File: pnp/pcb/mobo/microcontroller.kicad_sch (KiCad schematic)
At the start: 34 parts, among them J1 SWD Header, J32 BOOT_JUMPER, SW1 SW_Push, SW2 SW_Push, U1 STM32F407VETx, Y1 8MHz

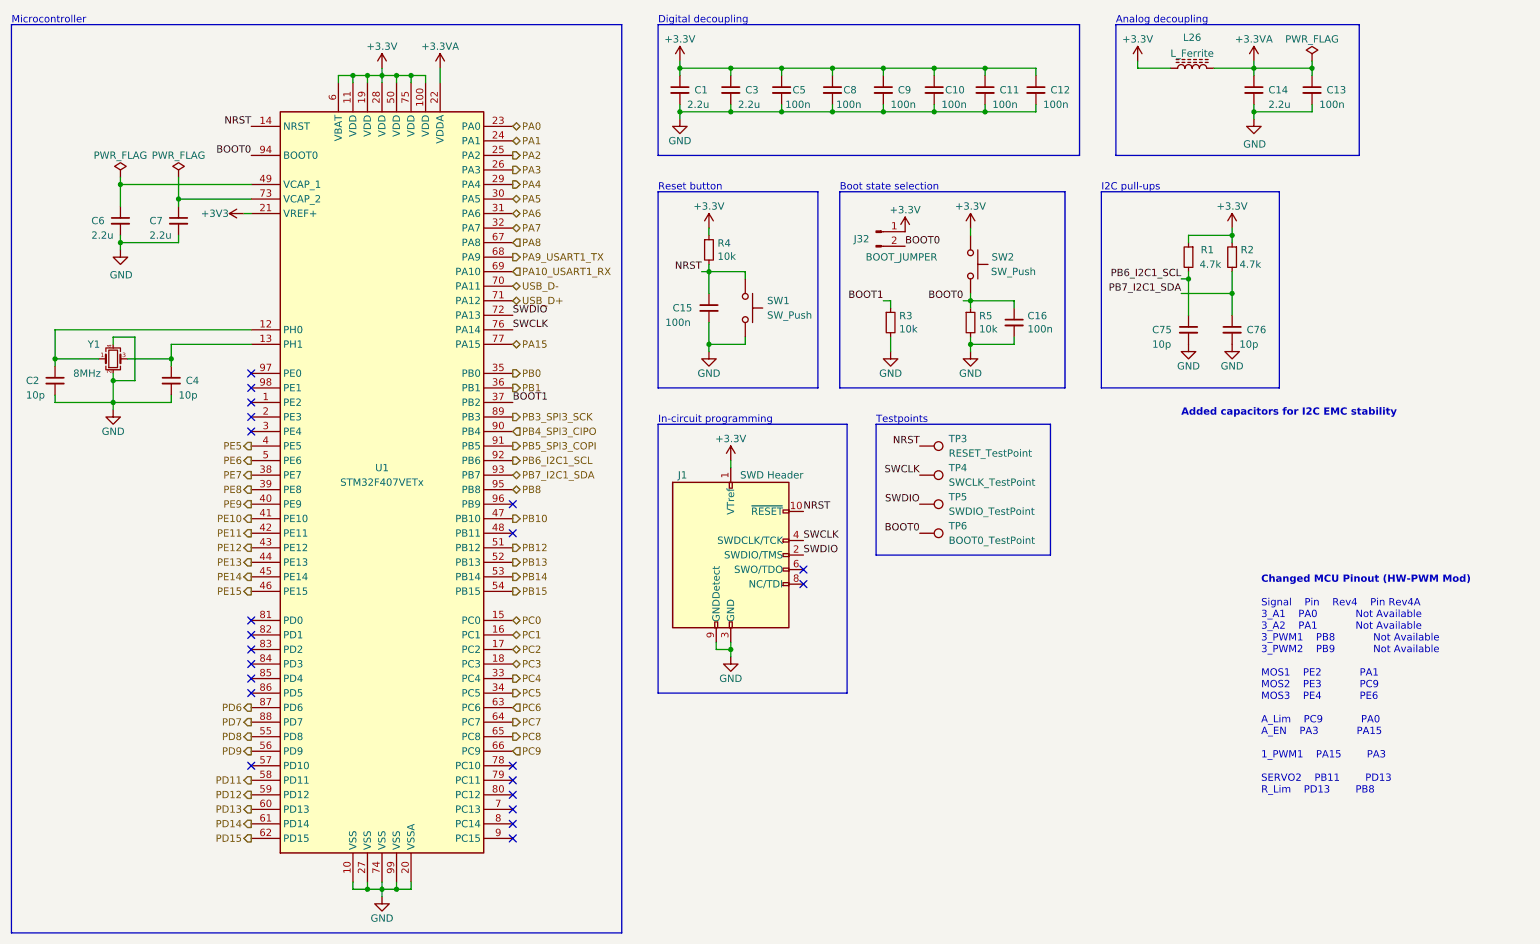
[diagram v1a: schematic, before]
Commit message: Redesign finished
Completed Board redesign and adding more EMC improvements.
Changed all the part numbers to have a Mouser orderable design (except the JST connectors)
All outputs generated
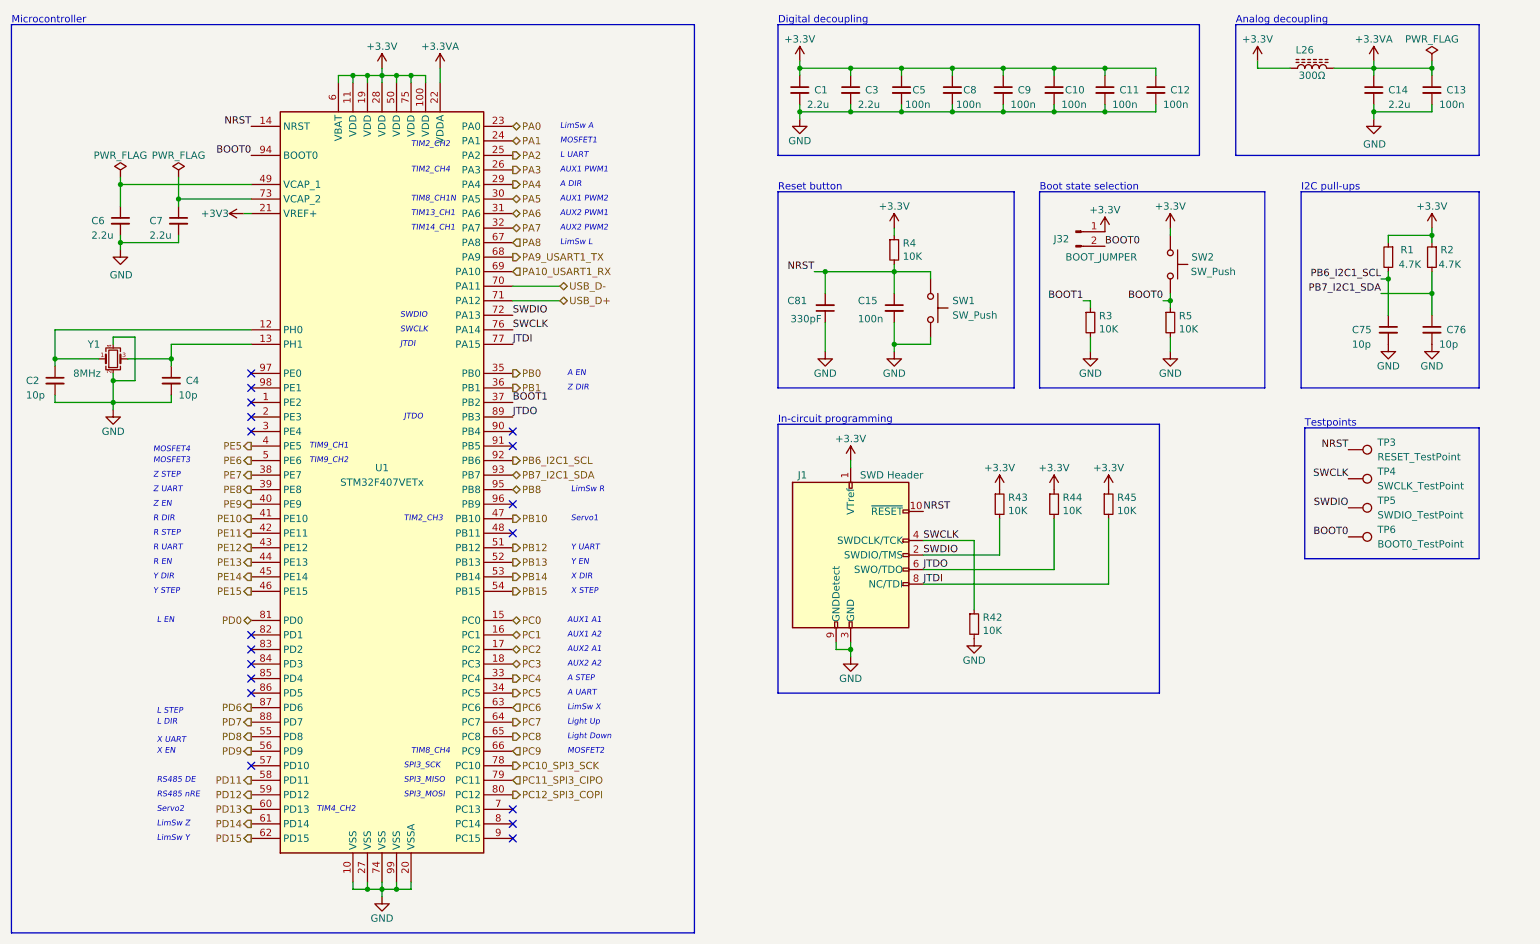
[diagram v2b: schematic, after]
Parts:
- removed C16: 100n, Capacitor_SMD:C_0805_2012Metric, symbol Device:C_Small
- removed L26: L_Ferrite, Inductor_SMD:L_0805_2012Metric, symbol Device:L_Ferrite
- added C81: 330pF, Capacitor_SMD:C_0805_2012Metric, symbol Device:C_Small
- added L26: 300Ω, Inductor_SMD:L_0805_2012Metric, symbol Device:300Ω
- added R42, R43, R44, R45: 10K, Resistor_SMD:R_0805_2012Metric, symbol Device:R_Small
- C1, C14, C3, C6, C7: Digikey 587-4961-1-ND -> (none); JLCPCB C49217 -> (none); LCSC C49217 -> (none); Mouser 963-UMK212ABJ225KG-T -> 810-C2012X5R1H225K
- C10, C11, C12, C13, C15, C5, C8, C9: Digikey 1276-1180-1-ND -> (none); JLCPCB C49678 -> (none); LCSC C360619 -> (none); Mouser 581-08055C104K -> 710-885012207098
- C2, C4, C75, C76: JLCPCB C1785 -> (none); LCSC C525280 -> (none); Mouser (none) -> 603-CC805JRNPO9BN100
- J1: LCSC C150517 -> (none); Mouser (none) -> 200-FTSH10501FDVKPTR
- J32: Mouser (none) -> 571-5-146280-2
- R1, R2: value 4.7k -> 4.7K; Digikey A129757CT-ND -> (none); JLCPCB C17673 -> (none); LCSC C17673 -> (none); Mouser 71-CRCW08054K70FKEAC -> 603-RC0805FR-104K7L
- R3, R4, R5: value 10k -> 10K; Digikey RMCF0805FT10K0CT-ND -> (none); JLCPCB C17414 -> (none); LCSC C115295 -> (none); Mouser 71-CRCW080510K0FKEAC -> 603-RC0805FR-1010KL
- SW1, SW2: Digikey SW415-ND -> (none); JLCPCB C83206 -> (none); LCSC C83206 -> (none); Mouser 653-B3S-1000P -> 769-EVP-BT1A4A000
- TP3, TP4, TP5, TP6: Mouser (none) -> -
- U1: JLCPCB C28730 -> (none); LCSC C28730 -> (none)
- Y1: JLCPCB C57131 -> (none); LCSC C518155 -> (none)
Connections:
- net PA15 is gone; now on net JTDI: U1.77 (PA15)
- net PB3_SPI3_SCK is gone; now on net JTDO: U1.89 (PB3)
- net +3.3VA: now also L26.2
- net +3V3: now also L26.1, R43.1, R44.1, R45.1
- net GND: now also C81.1, R42.2
- net NRST: now also C81.2
- net SWCLK: now also R42.1
- net SWDIO: now also R43.2
- net JTDO: now reaches J1.6 (SWO/TDO)
- net JTDO: now also R44.2
- net JTDI: now reaches J1.8 (NC/TDI)
- net JTDI: now also R45.2
- net PC10_SPI3_SCK: now reaches U1.78 (PC10)
- net PC11_SPI3_CIPO: now reaches U1.79 (PC11)
- net PC12_SPI3_COPI: now reaches U1.80 (PC12)
- net PD0: now reaches U1.81 (PD0)
- net PB4_SPI3_CIPO: no longer names the net of U1.90 (PB4)
- net PB5_SPI3_COPI: no longer names the net of U1.91 (PB5)
- no-connect marks 22 -> 18
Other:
- note added: "A DIR"
- note added: "A EN"
- note added: "A STEP"
- note added: "A UART"
- note added: "AUX1 A1"
- note added: "AUX1 A2"
- note added: "AUX1 PWM1"
- note added: "AUX1 PWM2"
- note added: "AUX2 A1"
- note added: "AUX2 A2"
- note added: "AUX2 PWM1"
- note added: "AUX2 PWM2"
- note added: "JTDI"
- note added: "JTDO"
- note added: "L DIR"
- note added: "L EN"
- note added: "L STEP"
- note added: "L UART"
- note added: "Light Down"
- note added: "Light Up"
- note added: "LimSw A"
- note added: "LimSw L"
- note added: "LimSw R"
- note added: "LimSw X"
- note added: "LimSw Y"
- note added: "LimSw Z"
- note added: "MOSFET1"
- note added: "MOSFET2"
- note added: "MOSFET3"
- note added: "MOSFET4"
- note added: "R DIR"
- note added: "R EN"
- note added: "R STEP"
- note added: "R UART"
- note added: "RS485 DE"
- note added: "RS485 nRE"
- note added: "SPI3_MISO"
- note added: "SPI3_MOSI"
- note added: "SPI3_SCK"
- note added: "SWCLK"
- note added: "SWDIO"
- note added: "Servo1"
- note added: "Servo2"
- note added: "TIM13_CH1"
- note added: "TIM14_CH1"
- note added: "TIM2_CH2"
- note added: "TIM2_CH3"
- note added: "TIM2_CH4"
- note added: "TIM4_CH2"
- note added: "TIM8_CH1N"
- note added: "TIM8_CH4"
- note added: "TIM9_CH1"
- note added: "TIM9_CH2"
- note added: "X DIR"
- note added: "X EN"
- note added: "X STEP"
- note added: "X UART"
- note added: "Y DIR"
- note added: "Y EN"
- note added: "Y STEP"
- note added: "Y UART"
- note added: "Z DIR"
- note added: "Z EN"
- note added: "Z STEP"
- note added: "Z UART"
- note removed: "Added capacitors for I2C EMC stability"
- note removed: "Changed MCU Pinout (HW-PWM Mod)"
- note removed: "Signal Pin Rev4 Pin Rev4A 3_A1 PA0 Not Available 3_A2 PA1 Not Available 3_PWM1 PB8 Not Available 3_PWM2 PB9 Not Available MOS1 PE2 PA1 MOS2 PE3 PC9 MOS3 PE4 PE6 A_Lim PC9 PA0 A_EN PA3 PA15 1_PWM1 PA15 PA3 SERVO2 PB11 PD13 R_Lim PD13 PB8"
- company: Opulo -> Opulo.io
- moved on the sheet: C1, C10, C11, C12, C13, C14, C15, C3, C5, C75, C76, C8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
